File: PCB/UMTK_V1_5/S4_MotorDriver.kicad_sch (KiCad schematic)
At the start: 17 parts, among them J1 Motor Out, J2 ESTOP, U1 DRV8873SPWPRQ1

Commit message: Routing
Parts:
- J1, J2: footprint TerminalBlock_Altech:Altech_AK100_1x02_P5.00mm -> Connector_Phoenix_MC_HighVoltage:PhoenixContact_MC_1,5_2-G-5.08_1x02_P5.08mm_Horizontal
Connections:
- net +12V: now also J2.2 (Pin_2); no longer J2.1 (Pin_1)
- net VM+: now also J1.2 (Pin_2); no longer J1.1 (Pin_1)
- net VM-: now also J1.1 (Pin_1); no longer J1.2 (Pin_2)
- net VMOTOR: now also J2.1 (Pin_1); no longer J2.2 (Pin_2)
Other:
- moved on the sheet: J1, J2
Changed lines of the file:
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@@
-	(wire
-		(pts
-			(xy 233.68 67.31) (xy 233.68 69.85)
-		)
-		(stroke
-			(width 0)
-			(type default)
-		)
-	)
 	(wire
 		(pts
@@
 	(wire
 		(pts
+			(xy 231.14 69.85) (xy 242.57 69.85)
+		)
+		(stroke
+			(width 0)
+			(type default)
+		)
+	)
+	(wire
+		(pts
 			(xy 113.03 156.21) (xy 113.03 148.59)
 		)
@@
 	(wire
 		(pts
-			(xy 220.98 72.39) (xy 245.11 72.39)
-		)
-		(stroke
-			(width 0)
-			(type default)
-		)
-	)
-	(wire
-		(pts
 			(xy 97.79 153.67) (xy 97.79 156.21)
 		)
@@
 	(wire
 		(pts
-			(xy 240.03 52.07) (xy 246.38 52.07)
-		)
-		(stroke
-			(width 0)
-			(type default)
-		)
-	)
-	(wire
-		(pts
 			(xy 81.28 140.97) (xy 93.98 140.97)
 		)
@@
 	(wire
 		(pts
-			(xy 233.68 69.85) (xy 245.11 69.85)
-		)
-		(stroke
-			(width 0)
-			(type default)
-		)
-	)
-	(wire
-		(pts
 			(xy 81.28 146.05) (xy 81.28 154.94)
 		)
@@
 	(wire
 		(pts
+			(xy 254 54.61) (xy 260.35 54.61)
+		)
+		(stroke
+			(width 0)
+			(type default)
+		)
+	)
+	(wire
+		(pts
 			(xy 182.88 161.29) (xy 182.88 163.83)
 		)
@@
 	(wire
 		(pts
-			(xy 240.03 54.61) (xy 246.38 54.61)
+			(xy 218.44 72.39) (xy 242.57 72.39)
 		)
 		(stroke
@@
 	(wire
 		(pts
+			(xy 231.14 67.31) (xy 231.14 69.85)
+		)
+		(stroke
+			(width 0)
+			(type default)
+		)
+	)
+	(wire
+		(pts
 			(xy 173.99 146.05) (xy 180.34 146.05)
 		)
@@
 		(pts
 			(xy 81.28 146.05) (xy 138.43 146.05)
+		)
+		(stroke
+			(width 0)
+			(type default)
+		)
+	)
+	(wire
+		(pts
+			(xy 254 52.07) (xy 260.35 52.07)
 		)
 		(stroke
@@
 		)
 	)
-	(label "VM-"
-		(at 246.38 54.61 0)
+	(label "SR - Slew Rate Adjust"
+		(at 85.09 146.05 0)
 		(fields_autoplaced yes)
 		(effects
@@
 		)
 	)
-	(label "SR - Slew Rate Adjust"
-		(at 85.09 146.05 0)
+	(label "VM+"
+		(at 181.61 128.27 0)
 		(fields_autoplaced yes)
 		(effects
@@
 	)
 	(label "VM+"
-		(at 181.61 128.27 0)
+		(at 260.35 52.07 0)
 		(fields_autoplaced yes)
 		(effects
@@
 		)
 	)
-	(label "VM+"
-		(at 246.38 52.07 0)
+	(label "VM-"
+		(at 260.35 54.61 0)
 		(fields_autoplaced yes)
 		(effects
@@
 	(global_label "VMOTOR"
 		(shape input)
-		(at 220.98 72.39 180)
+		(at 215.9 110.49 180)
 		(fields_autoplaced yes)
 		(effects
@@
 		)
 		(property "Intersheetrefs" "${INTERSHEET_REFS}"
-			(at 210.5562 72.39 0)
+			(at 205.4762 110.49 0)
 			(effects
 				(font
@@
 	(global_label "VMOTOR"
 		(shape input)
-		(at 215.9 110.49 180)
+		(at 218.44 72.39 180)
 		(fields_autoplaced yes)
 		(effects
@@
 		)
 		(property "Intersheetrefs" "${INTERSHEET_REFS}"
-			(at 205.4762 110.49 0)
+			(at 208.0162 72.39 0)
 			(effects
 				(font
@@
 	)
 	(symbol
+		(lib_id "power:+12V")
+		(at 231.14 67.31 0)
+		(unit 1)
+		(exclude_from_sim no)
+		(in_bom yes)
+		(on_board yes)
+		(dnp no)
+		(fields_autoplaced yes)
+		(property "Reference" "#PWR07"
+			(at 231.14 71.12 0)
+			(effects
+				(font
+					(size 1.27 1.27)
+				)
+				(hide yes)
+			)
+		)
+		(property "Value" "+12V"
+			(at 231.14 62.23 0)
+			(effects
+				(font
+					(size 1.27 1.27)
+				)
+			)
+		)
+		(property "Footprint" ""
+			(at 231.14 67.31 0)
+			(effects
+				(font
+					(size 1.27 1.27)
+				)
+				(hide yes)
+			)
+		)
+		(property "Datasheet" ""
+			(at 231.14 67.31 0)
+			(effects
+				(font
+					(size 1.27 1.27)
+				)
+				(hide yes)
+			)
+		)
+		(property "Description" "Power symbol creates a global label with name \"+12V\""
+			(at 231.14 67.31 0)
+			(effects
+				(font
+					(size 1.27 1.27)
+				)
+				(hide yes)
+			)
+		)
+		(pin "1"
+		)
+		(instances
+			(project "UMTK"
+				(path "/2bf3ea67-58b8-47b3-a768-ea6950b40edf/429db1c7-ec58-4147-903c-f97ceea1f1c2"
+					(reference "#PWR07")
+					(unit 1)
+				)
+			)
+		)
+	)
+	(symbol
 		(lib_id "power:GND")
 		(at 199.39 156.21 0)
@@
 	(symbol
 		(lib_id "Connector:Screw_Terminal_01x02")
-		(at 234.95 52.07 0)
-		(mirror y)
+		(at 248.92 54.61 180)
 		(unit 1)
 		(exclude_from_sim no)
@@
 		(dnp no)
 		(property "Reference" "J1"
-			(at 234.95 49.53 0)
+			(at 248.92 57.15 0)
 			(effects
 				(font
@@
 		)
 		(property "Value" "Motor Out"
-			(at 234.95 57.15 0)
-			(effects
-				(font
-					(size 1.27 1.27)
-				)
-			)
-		)
-		(property "Footprint" "TerminalBlock_Altech:Altech_AK100_1x02_P5.00mm"
-			(at 234.95 52.07 0)
+			(at 248.92 49.53 0)
+			(effects
+				(font
+					(size 1.27 1.27)
+				)
+			)
+		)
+		(property "Footprint" "Connector_Phoenix_MC_HighVoltage:PhoenixContact_MC_1,5_2-G-5.08_1x02_P5.08mm_Horizontal"
+			(at 248.92 54.61 0)
 			(effects
 				(font
@@
 		)
 		(property "Datasheet" "~"
-			(at 234.95 52.07 0)
+			(at 248.92 54.61 0)
 			(effects
 				(font
@@
 		)
 		(property "Description" "Generic screw terminal, single row, 01x02, script generated (kicad-library-utils/schlib/autogen/connector/)"
-			(at 234.95 52.07 0)
+			(at 248.92 54.61 0)
 			(effects
 				(font
@@
 	)
 	(symbol
-		(lib_id "power:+12V")
-		(at 233.68 67.31 0)
-		(unit 1)
-		(exclude_from_sim no)
-		(in_bom yes)
-		(on_board yes)
-		(dnp no)
-		(fields_autoplaced yes)
-		(property "Reference" "#PWR018"
-			(at 233.68 71.12 0)
-			(effects
-				(font
-					(size 1.27 1.27)
-				)
-				(hide yes)
-			)
-		)
-		(property "Value" "+12V"
-			(at 233.68 62.23 0)
-			(effects
-				(font
-					(size 1.27 1.27)
-				)
-			)
-		)
-		(property "Footprint" ""
-			(at 233.68 67.31 0)
-			(effects
-				(font
-					(size 1.27 1.27)
-				)
-				(hide yes)
-			)
-		)
-		(property "Datasheet" ""
-			(at 233.68 67.31 0)
-			(effects
-				(font
-					(size 1.27 1.27)
-				)
-				(hide yes)
-			)
-		)
-		(property "Description" "Power symbol creates a global label with name \"+12V\""
-			(at 233.68 67.31 0)
-			(effects
-				(font
-					(size 1.27 1.27)
-				)
-				(hide yes)
-			)
-		)
-		(pin "1"
-		)
-		(instances
-			(project ""
-				(path "/2bf3ea67-58b8-47b3-a768-ea6950b40edf/429db1c7-ec58-4147-903c-f97ceea1f1c2"
-					(reference "#PWR018")
-					(unit 1)
-				)
-			)
-		)
-	)
-	(symbol
 		(lib_id "Device:C")
 		(at 201.93 127 180)
@@
 	(symbol
 		(lib_id "Connector:Screw_Terminal_01x02")
-		(at 250.19 69.85 0)
+		(at 247.65 72.39 0)
+		(mirror x)
 		(unit 1)
 		(exclude_from_sim no)
@@
 		(dnp no)
 		(property "Reference" "J2"
-			(at 250.19 67.31 0)
+			(at 247.65 74.93 0)
 			(effects
 				(font
@@
 		)
 		(property "Value" "ESTOP"
-			(at 250.19 74.93 0)
-			(effects
-				(font
-					(size 1.27 1.27)
-				)
-			)
-		)
-		(property "Footprint" "TerminalBlock_Altech:Altech_AK100_1x02_P5.00mm"
-			(at 250.19 69.85 0)
+			(at 247.65 67.31 0)
+			(effects
+				(font
+					(size 1.27 1.27)
+				)
+			)
+		)
+		(property "Footprint" "Connector_Phoenix_MC_HighVoltage:PhoenixContact_MC_1,5_2-G-5.08_1x02_P5.08mm_Horizontal"
+			(at 247.65 72.39 0)
 			(effects
 				(font
@@
 		)
 		(property "Datasheet" "~"
-			(at 250.19 69.85 0)
+			(at 247.65 72.39 0)
 			(effects
 				(font
@@
 		)
 		(property "Description" "Generic screw terminal, single row, 01x02, script generated (kicad-library-utils/schlib/autogen/connector/)"
-			(at 250.19 69.85 0)
-			(effects
-				(font
+			(at 247.65 72.39 0)
+			(effects
+				(font

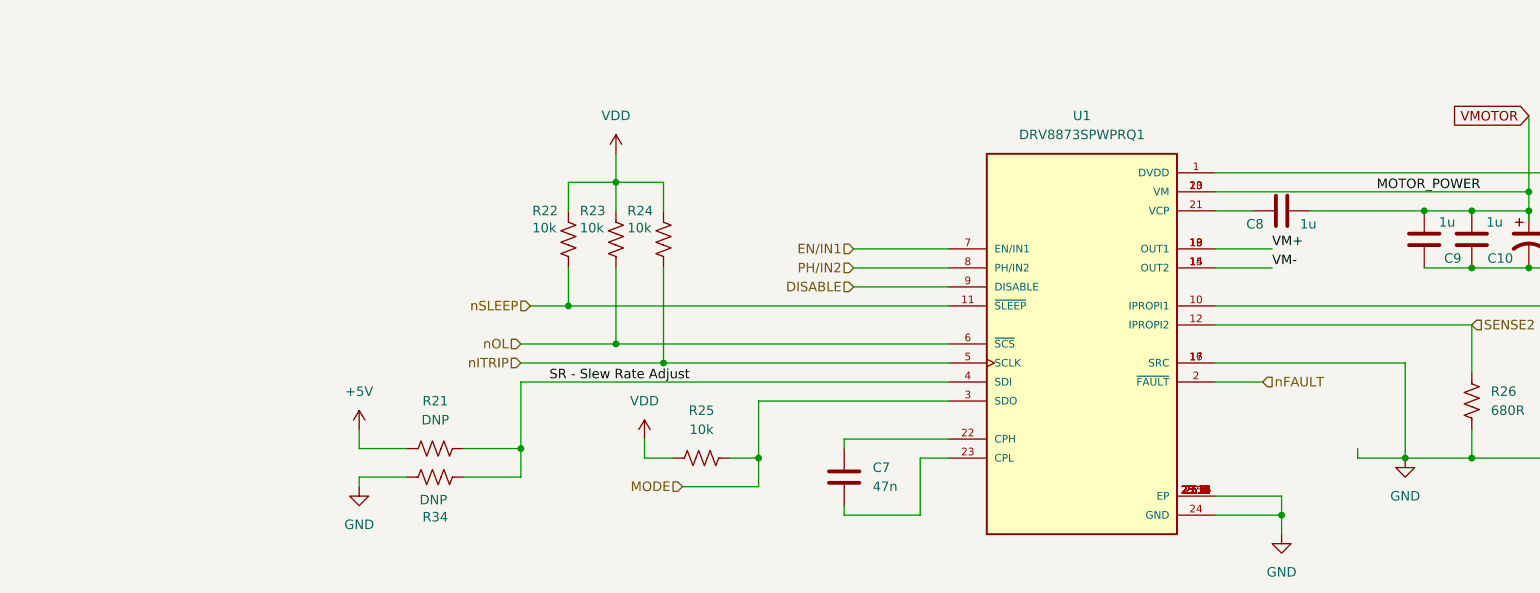
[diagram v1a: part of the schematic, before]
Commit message: Added Sinkscreen Annotations, PCB Done for now
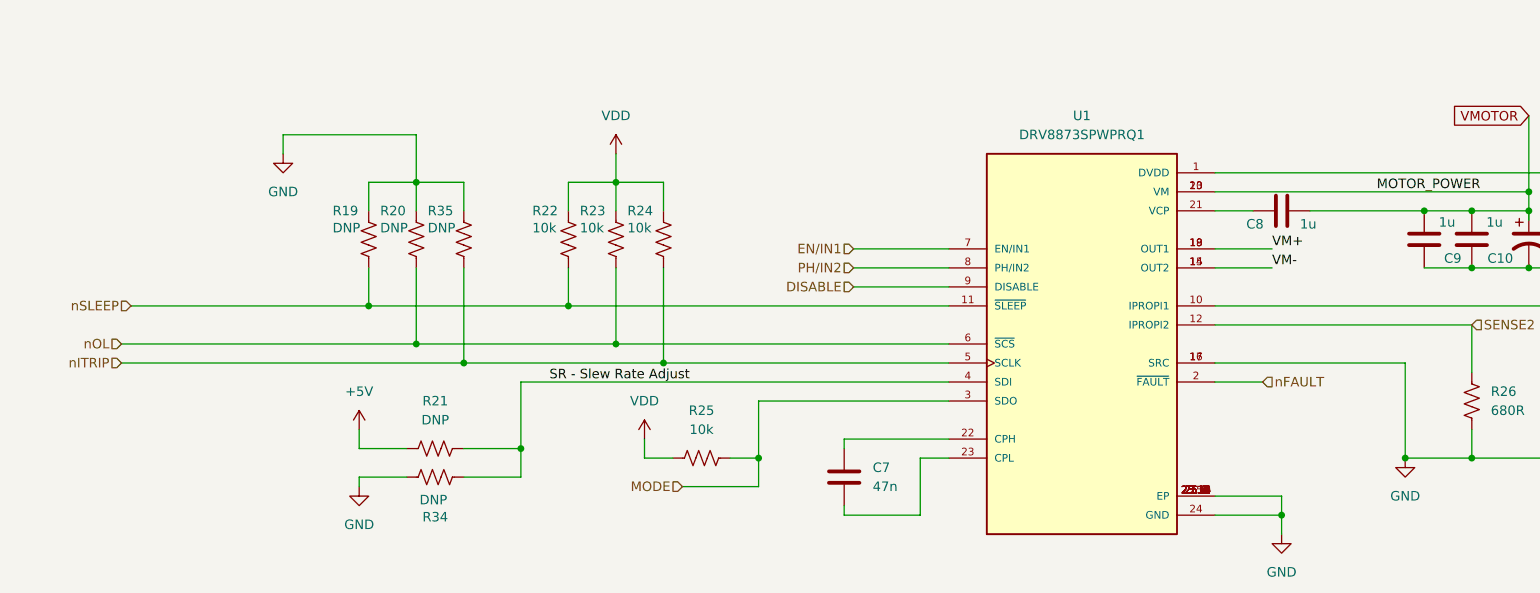
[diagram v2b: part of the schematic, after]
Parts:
- added R19, R20, R35: DNP, Resistor_SMD:R_0402_1005Metric, symbol Device:R_US
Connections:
- net GND: now also R19.2, R20.2, R35.2
- net nITRIP: now also R35.1
- net nOL: now also R20.1
- net nSLEEP: now also R19.1

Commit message: Assigning JLC
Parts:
- C10, C9: value 1u -> 1u 100v
- C12, C8: value 1u -> 1u 16v
- R24: value 10k -> DNP
- R35: value DNP -> 10K
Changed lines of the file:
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@@
 			)
 		)
-		(property "Value" "1u"
+		(property "Value" "1u 16v"
 			(at 225.806 120.904 0)
 			(effects
@@
 			)
 		)
-		(property "Value" "1u"
-			(at 204.978 124.714 0)
+		(property "Value" "1u 100v"
+			(at 198.12 124.46 0)
 			(effects
 				(font
@@
 			)
 		)
-		(property "Value" "1u"
+		(property "Value" "1u 16v"
 			(at 186.436 124.968 90)
 			(effects
@@
 			)
 		)
-		(property "Value" "1u"
-			(at 211.328 124.714 0)
+		(property "Value" "1u 100v"
+			(at 209.296 124.714 0)
 			(effects
 				(font
@@
 			)
 		)
-		(property "Value" "DNP"
+		(property "Value" "10K"
 			(at 68.834 125.476 0)
 			(effects
@@
 			)
 		)
-		(property "Value" "10k"
+		(property "Value" "DNP"
 			(at 95.504 125.476 0)
 			(effects

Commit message: Routing and JLC Assignment Done
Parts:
- C10, C9: value 1u 100v -> 1u hv; footprint Capacitor_SMD:C_0603_1608Metric -> Capacitor_SMD:C_1206_3216Metric
- C11: value 100u -> 100u hv
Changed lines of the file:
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@@
 			)
 		)
-		(property "Value" "1u 100v"
+		(property "Value" "1u hv"
 			(at 198.12 124.46 0)
 			(effects
@@
 			)
 		)
-		(property "Footprint" "Capacitor_SMD:C_0603_1608Metric"
+		(property "Footprint" "Capacitor_SMD:C_1206_3216Metric"
 			(at 200.9648 123.19 0)
 			(effects
@@
 			)
 		)
-		(property "Value" "1u 100v"
+		(property "Value" "1u hv"
 			(at 209.296 124.714 0)
 			(effects
@@
 			)
 		)
-		(property "Footprint" "Capacitor_SMD:C_0603_1608Metric"
+		(property "Footprint" "Capacitor_SMD:C_1206_3216Metric"
 			(at 207.3148 123.19 0)
 			(effects
@@
 			)
 		)
-		(property "Value" "100u"
+		(property "Value" "100u hv"
 			(at 219.71 127.6349 0)
 			(effects

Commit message: Bug fixes and add dummy headers for DFM
Fix:
- Power jack footprint incorrect for high current jack
- Motor and Estop terminal hole size too small
- Added designator and position for arduino headers for DFM
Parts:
- J1, J2: footprint Connector_Phoenix_MC_HighVoltage:PhoenixContact_MC_1,5_2-G-5.08_1x02_P5.08mm_Horizontal -> Connector_Phoenix_MSTB:PhoenixContact_MSTBA_2,5_2-G-5,08_1x02_P5.08mm_Horizontal
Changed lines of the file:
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@@
 			)
 		)
-		(property "Footprint" "Connector_Phoenix_MC_HighVoltage:PhoenixContact_MC_1,5_2-G-5.08_1x02_P5.08mm_Horizontal"
+		(property "Footprint" "Connector_Phoenix_MSTB:PhoenixContact_MSTBA_2,5_2-G-5,08_1x02_P5.08mm_Horizontal"
 			(at 248.92 54.61 0)
 			(effects
@@
 			)
 		)
-		(property "Footprint" "Connector_Phoenix_MC_HighVoltage:PhoenixContact_MC_1,5_2-G-5.08_1x02_P5.08mm_Horizontal"
+		(property "Footprint" "Connector_Phoenix_MSTB:PhoenixContact_MSTBA_2,5_2-G-5,08_1x02_P5.08mm_Horizontal"
 			(at 247.65 72.39 0)
 			(effects

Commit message: Make simple components bigger
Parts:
- C7: footprint Capacitor_SMD:C_0402_1005Metric -> Capacitor_SMD:C_0603_1608Metric
- R19, R20, R21, R22, R23, R24, R25, R34, R35: footprint Resistor_SMD:R_0402_1005Metric -> Resistor_SMD:R_0603_1608Metric
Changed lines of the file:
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@@
 			)
 		)
-		(property "Footprint" "Resistor_SMD:R_0402_1005Metric"
+		(property "Footprint" "Resistor_SMD:R_0603_1608Metric"
 			(at 66.294 126.746 90)
 			(effects
@@
 			)
 		)
-		(property "Footprint" "Capacitor_SMD:C_0402_1005Metric"
+		(property "Footprint" "Capacitor_SMD:C_0603_1608Metric"
 			(at 125.4252 162.56 0)
 			(effects
@@
 			)
 		)
-		(property "Footprint" "Resistor_SMD:R_0402_1005Metric"
+		(property "Footprint" "Resistor_SMD:R_0603_1608Metric"
 			(at 69.596 155.956 90)
 			(effects
@@
 			)
 		)
-		(property "Footprint" "Resistor_SMD:R_0402_1005Metric"
+		(property "Footprint" "Resistor_SMD:R_0603_1608Metric"
 			(at 59.944 126.746 90)
 			(effects
@@
 			)
 		)
-		(property "Footprint" "Resistor_SMD:R_0402_1005Metric"
+		(property "Footprint" "Resistor_SMD:R_0603_1608Metric"
 			(at 70.104 157.734 90)
 			(effects
@@
 			)
 		)
-		(property "Footprint" "Resistor_SMD:R_0402_1005Metric"
+		(property "Footprint" "Resistor_SMD:R_0603_1608Metric"
 			(at 72.644 126.746 90)
 			(effects
@@
 			)
 		)
-		(property "Footprint" "Resistor_SMD:R_0402_1005Metric"
+		(property "Footprint" "Resistor_SMD:R_0603_1608Metric"
 			(at 99.314 126.746 90)
 			(effects
@@
 			)
 		)
-		(property "Footprint" "Resistor_SMD:R_0402_1005Metric"
+		(property "Footprint" "Resistor_SMD:R_0603_1608Metric"
 			(at 105.664 155.194 90)
 			(effects
@@
 			)
 		)
-		(property "Footprint" "Resistor_SMD:R_0402_1005Metric"
+		(property "Footprint" "Resistor_SMD:R_0603_1608Metric"
 			(at 86.614 126.746 90)
 			(effects
@@
 			)
 		)
-		(property "Footprint" "Resistor_SMD:R_0402_1005Metric"
+		(property "Footprint" "Resistor_SMD:R_0603_1608Metric"
 			(at 92.964 126.746 90)
 			(effects

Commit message: Update Firmware
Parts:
- R25: value 10k -> 0R
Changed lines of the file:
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@@
 			)
 		)
-		(property "Value" "10k"
+		(property "Value" "0R"
 			(at 105.41 152.4 90)
 			(effects

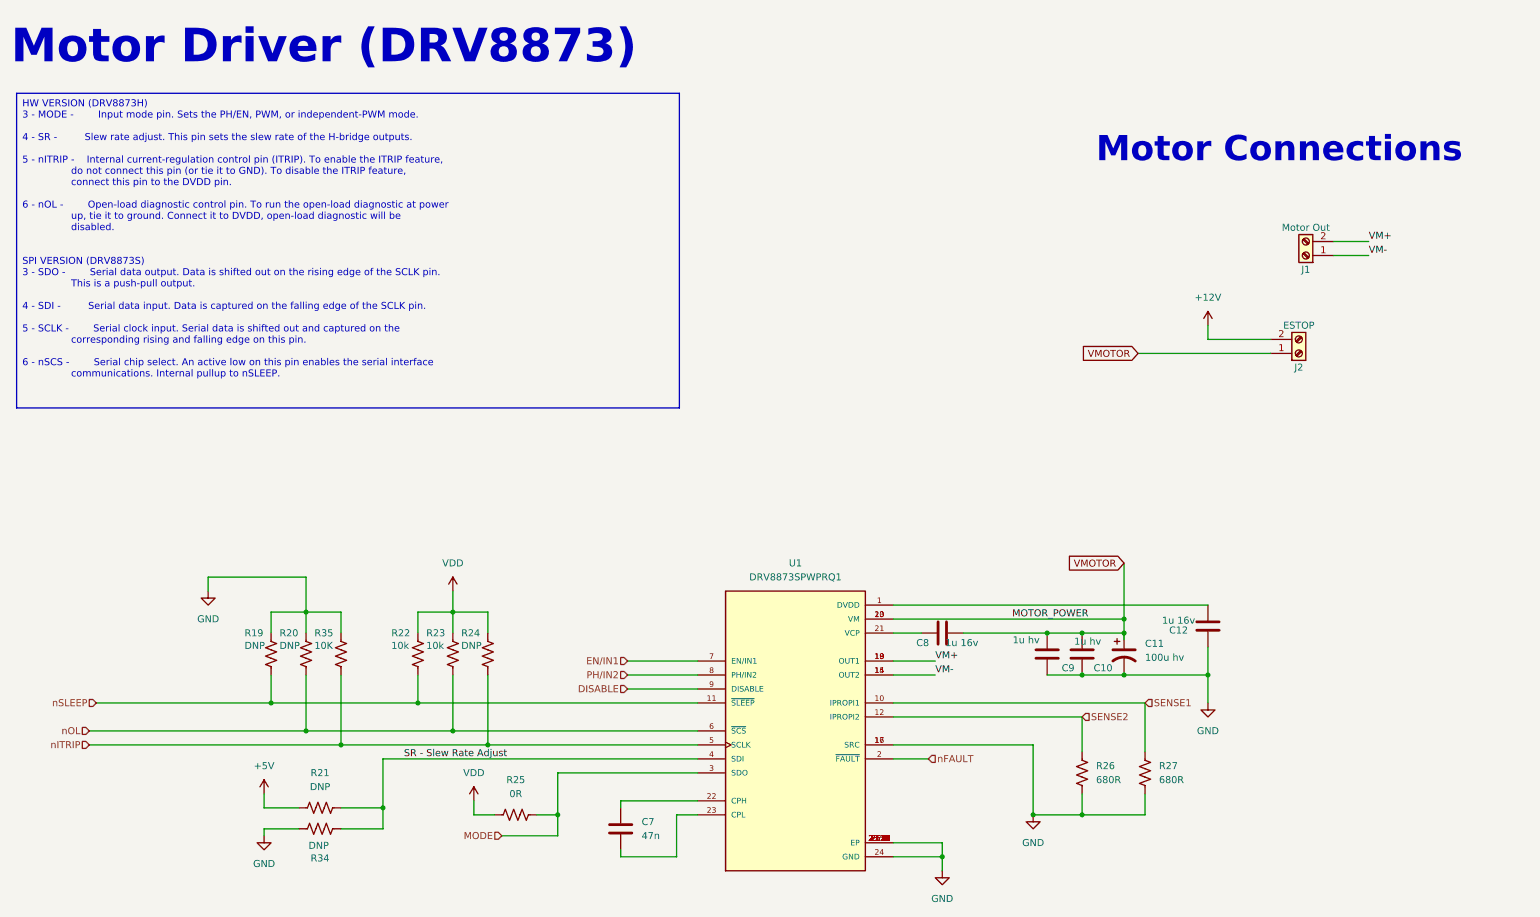
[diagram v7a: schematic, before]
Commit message: PCB Revision
- Add filter for 7seg power again
- Add low pass filter for output of motor power sense
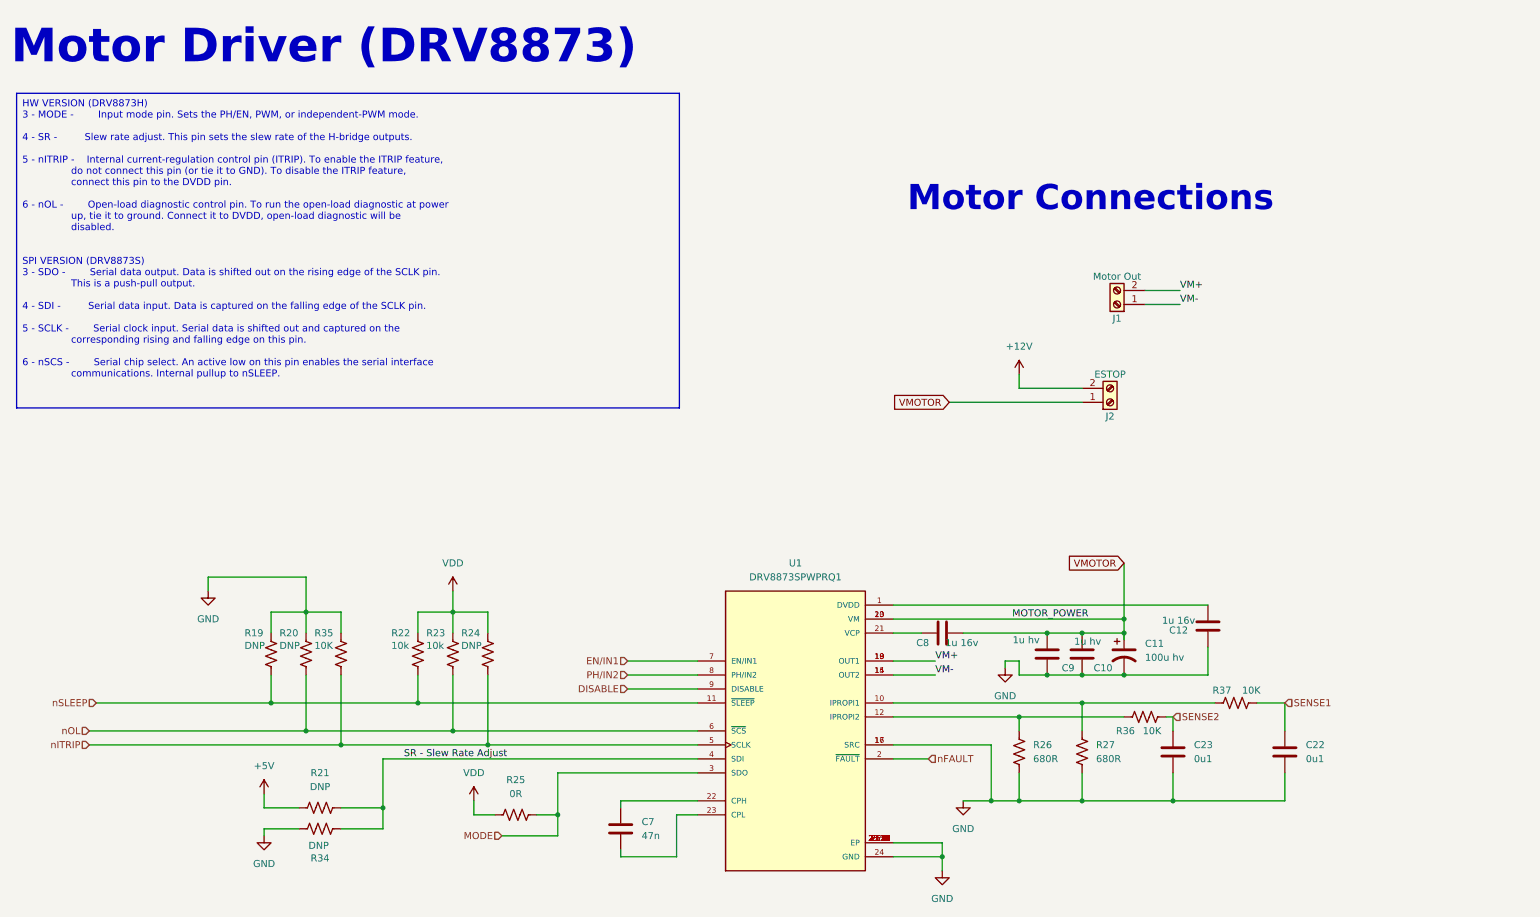
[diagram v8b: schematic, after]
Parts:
- added C22, C23: 0u1, Capacitor_SMD:C_0603_1608Metric, symbol Device:C
- added R36, R37: 10K, Resistor_SMD:R_0603_1608Metric, symbol Device:R_US
- J1: footprint Connector_Phoenix_MSTB:PhoenixContact_MSTBA_2,5_2-G-5,08_1x02_P5.08mm_Horizontal -> Connector_Phoenix_MC:PhoenixContact_MC_1,5_2-G-3.81_1x02_P3.81mm_Horizontal
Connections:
- net GND: now also C22.2, C23.2
- net SENSE1: now also C22.1, R37.2; no longer R27.2, U1.10 (IPROPI1)
- net SENSE2: now also C23.1, R36.2; no longer R26.2, U1.12 (IPROPI2)
- new net: R27.2, R37.1, U1.10 (IPROPI1)
- new net: R26.2, R36.1, U1.12 (IPROPI2)
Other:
- moved on the sheet: J1, J2, R26, R27
